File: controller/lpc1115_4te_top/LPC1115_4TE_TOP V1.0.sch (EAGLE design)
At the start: 106 parts, among them P2 ISP, Q1 BC856, Q2 BCP52, Q3 BC547C, U1 LPC1115FBD48, U2 BD9G101, U3 XO32 12MHz, X1 12MHz

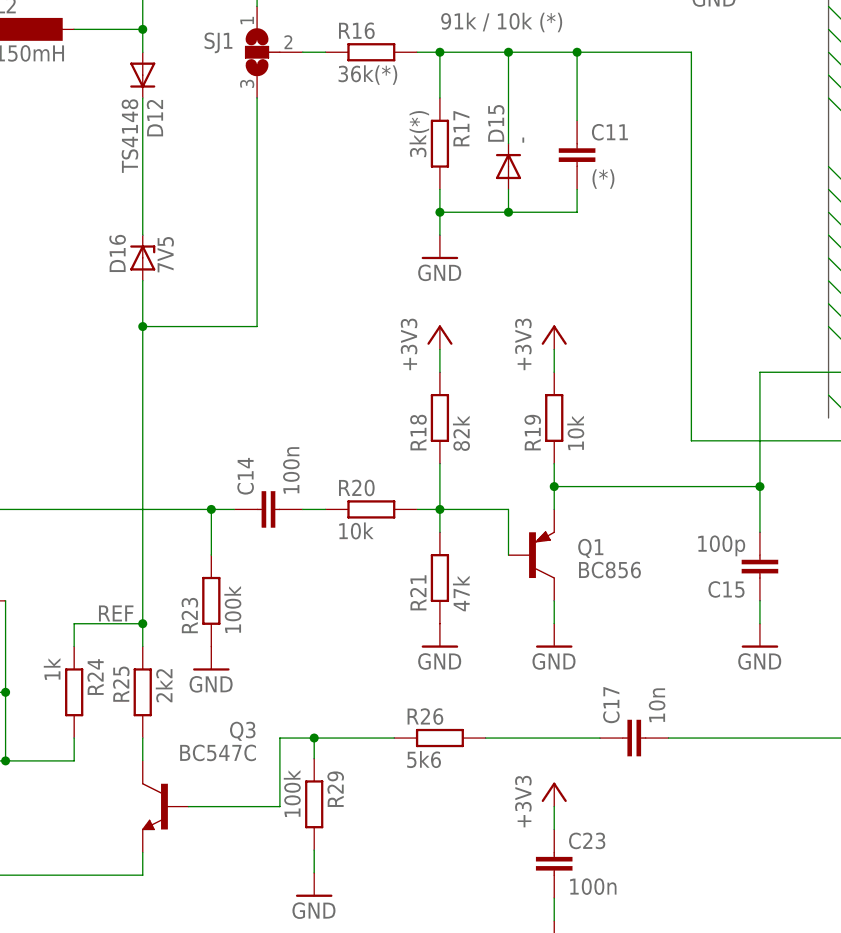
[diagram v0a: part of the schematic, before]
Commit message: Korrekturen am Controller und Ergänzung der BOMs und 3D-Bauteile
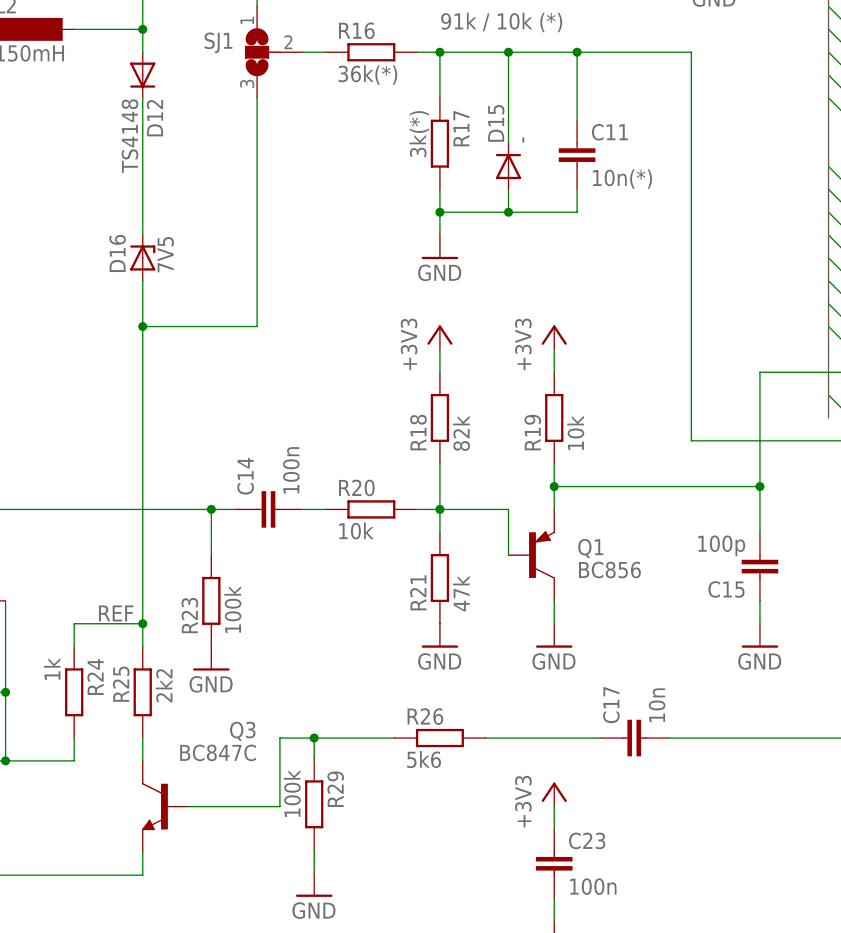
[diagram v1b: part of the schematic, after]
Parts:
- C11: value (*) -> 10n(*)
- Q3: value BC547C -> BC847C
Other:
- note added: "D13 mit SMAJ40C nur dann notwendig, wenn nicht näher EIB Steckverbinder eine vorhanden ist."
- note added: "Quarz versus Oszillator: Entweder Oszillator U3 mit C18, C22 bestücken oder Quarz X1 mit C20+C21 Nicht beide! (Quarz mit 10pF Lastkap)"
- note added: "mögliche Dioden: (sinnvolle Auslegung: Überlebt einen Ausgangskurzschluss) RB060M SOD123 schwer zu beschaffen - 2A Iav MBR0540 SOD123 nicht dauerkurzschlussfest - 0,5A Iav PMEG6010CEH SOD123 - 1A Iav STPS1L60, MBRS140, etc SMB - 1A Iav"
- note removed: "D13 mit SMAJ40C nur dann notwendig, wenn nicht näher am Stecker eine vorhanden ist."
- note removed: "Quarz versus Oszillator: Entweder Oszillator Q4 bestücken oder Quarz XTAL1 mit C5+C18 Nicht beide! (Quarz mit 10pF Lastkap)"
- note removed: "mögliche Dioden: RB060M SOD123 schwer zu beschaffen - 2A Iav MBR0540 SOD123 nicht dauerkurzschlussfest - 0,5A Iav PMEG6010CEH SOD123 - 1A Iav STPS1L60, MBRS140, etc SMB - 1A Iav"
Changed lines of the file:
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@@
 <part name="R20" library="rcl" deviceset="R-EU_" device="R0805M" value="10k"/>
 <part name="C9" library="rcl" deviceset="C-EU" device="C0805M" value="10n"/>
-<part name="Q3" library="transistor" deviceset="BC847" device="" value="BC547C"/>
+<part name="Q3" library="transistor" deviceset="BC847" device="" value="BC847C"/>
 <part name="GND32" library="supply1" deviceset="GND" device=""/>
 <part name="GND42" library="supply1" deviceset="GND" device=""/>
@@
 <part name="LED1" library="led" deviceset="LED" device="SMT1206"/>
 <part name="D13" library="semicon-smd-ipc" deviceset="D-" device="SMB"/>
-<part name="C11" library="rcl" deviceset="C-EU" device="C0805M" value="(*)"/>
+<part name="C11" library="rcl" deviceset="C-EU" device="C0805M" value="10n(*)"/>
 <part name="C22" library="rcl" deviceset="C-EU" device="C0805M" value="220p"/>
 <part name="C18" library="rcl" deviceset="C-EU" device="C0805M" value="100p"/>
@@
 <text x="314.96" y="134.62" size="1.778" layer="104">D13 mit SMAJ40C nur dann
 notwendig, wenn nicht näher
-am Stecker eine vorhanden ist.</text>
+EIB Steckverbinder eine
+vorhanden ist.</text>
 <text x="231.14" y="200.66" size="1.778" layer="104" rot="R180">Power LED (LED4+R20)
 ist optional</text>
 <text x="139.7" y="20.32" size="1.778" layer="104">Quarz versus Oszillator:
-Entweder Oszillator Q4 bestücken
-oder Quarz XTAL1 mit C5+C18
+Entweder Oszillator U3 mit C18, C22
+bestücken oder Quarz X1 mit C20+C21
 Nicht beide!
 (Quarz mit 10pF Lastkap)</text>
@@
 <wire x1="88.9" y1="53.34" x2="66.04" y2="33.02" width="0.1524" layer="104" style="shortdash"/>
 <text x="7.62" y="251.46" size="1.778" layer="104">(*): Bestückung applikationsabhängig</text>
-<text x="114.3" y="187.96" size="1.778" layer="104">mögliche Dioden:
+<text x="106.68" y="187.96" size="1.778" layer="104">mögliche Dioden:
+(sinnvolle Auslegung: Überlebt einen Ausgangskurzschluss)
 RB060M SOD123 schwer zu beschaffen - 2A Iav
 MBR0540 SOD123 nicht dauerkurzschlussfest - 0,5A Iav
